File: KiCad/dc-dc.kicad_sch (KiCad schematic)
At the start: 60 parts, among them Q1 NMOS, Q2 NMOS, Q3 NMOS, Q4 NMOS, U3 LT8390xFE

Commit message: new layout
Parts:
- removed NT1, NT2, NT3, NT4: NetTie_2, symbol Device:NetTie_2
- removed R5: 5m, Resistor_SMD:R_1206_3216Metric, symbol Device:R
- removed R6: 20m, Resistor_SMD:R_1206_3216Metric, symbol Device:R
- added HS1: 960-21-18-D-AB-0, Library:960-21-xx-D, symbol Mechanical:Heatsink
- added R5: 5m, Resistor_SMD:R_Shunt_Ohmite_LVK12, symbol Device:R_Shunt
- added R6: 12m, Resistor_SMD:R_Shunt_Ohmite_LVK12, symbol Device:R_Shunt
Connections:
- net ISN: now also R6.3
- net ISP: now also R6.2
- net LSN: now also R5.2
- net LSP: now also R5.3
- net SW1: now also R5.4
- net VOUT: now also R6.4
- net VOUTa: now reaches C15.1, C16.1, C17.1, C18.1, C19.1, Q3.1 (D)
- net VOUTa: now also R6.1
- net SW1a: now reaches L1.1
- net SW1a: now also R5.1

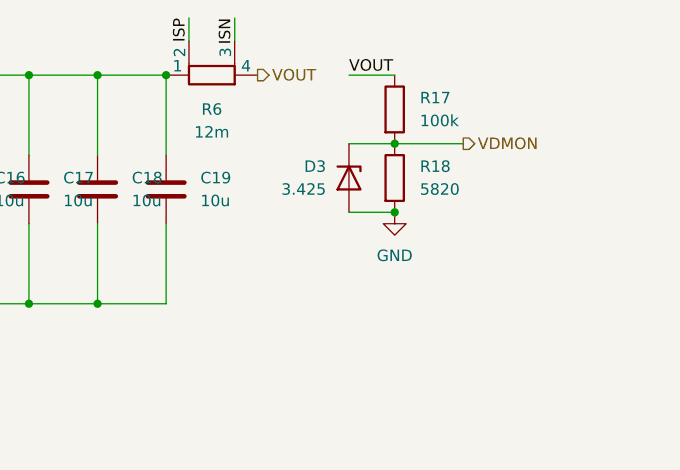
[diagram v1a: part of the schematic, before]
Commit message: multi sheet redesign
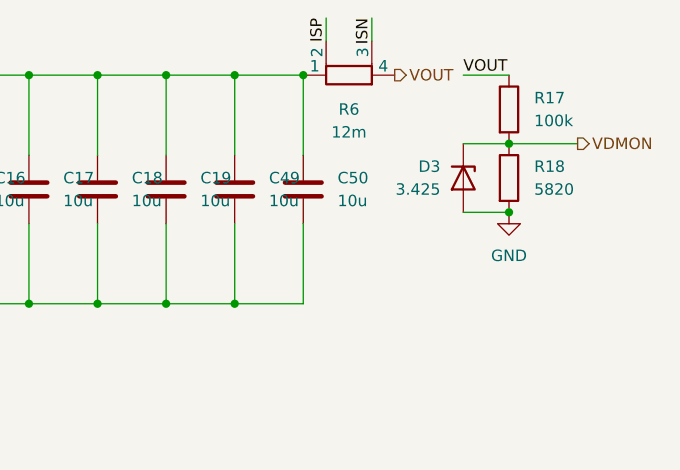
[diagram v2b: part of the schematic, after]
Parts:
- added C49, C50: 10u, Capacitor_SMD:C_1206_3216Metric, symbol Device:C
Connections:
- net GND: now also C49.2, C50.2
- net VOUTa: now also C49.1, C50.1
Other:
- moved on the sheet: D3, R17, R18, R6

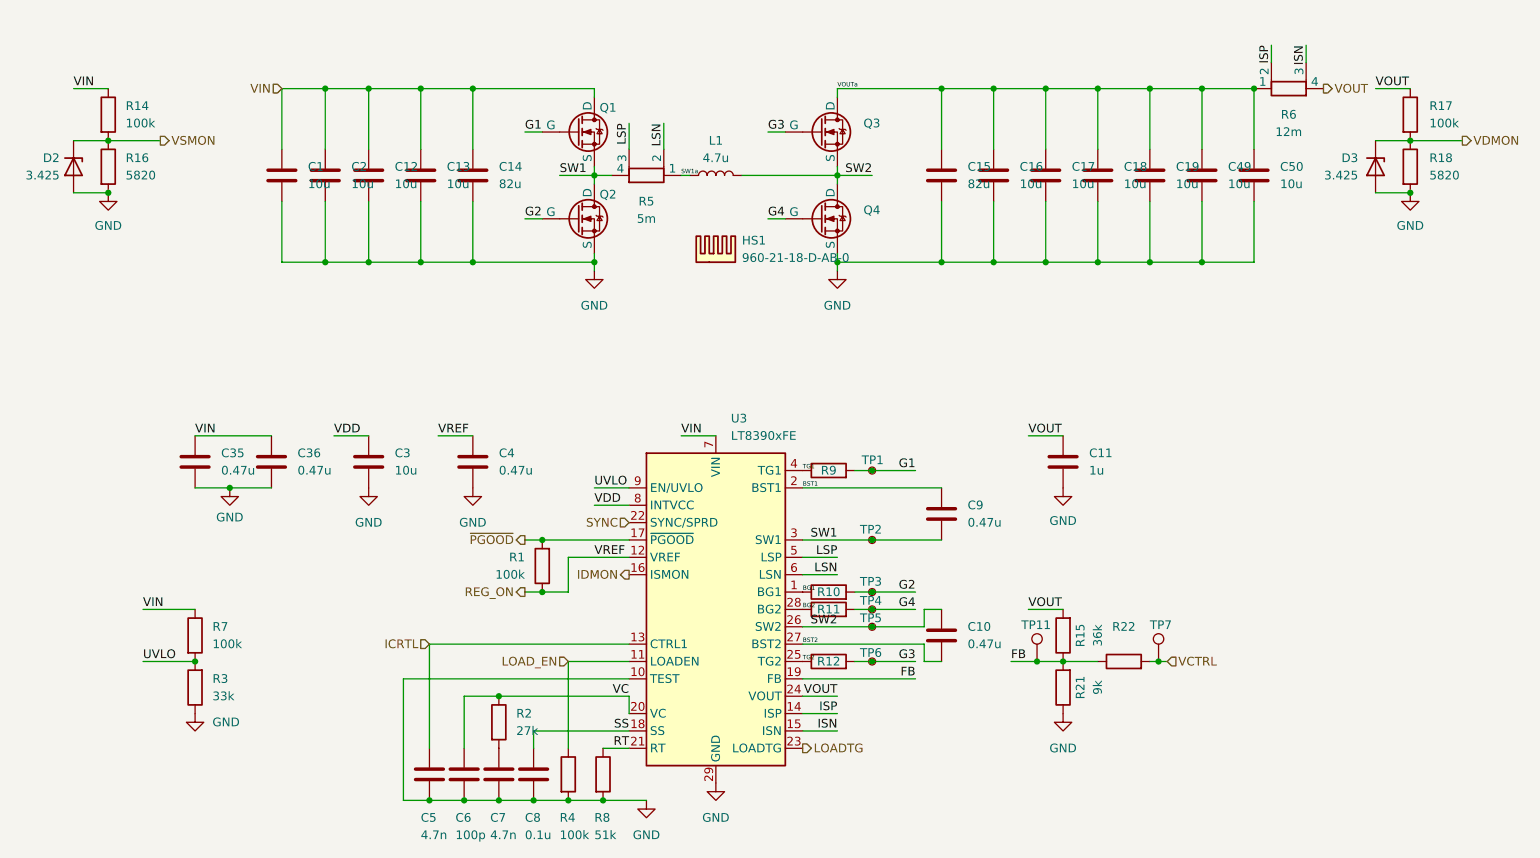
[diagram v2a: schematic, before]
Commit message: standalone regulator core
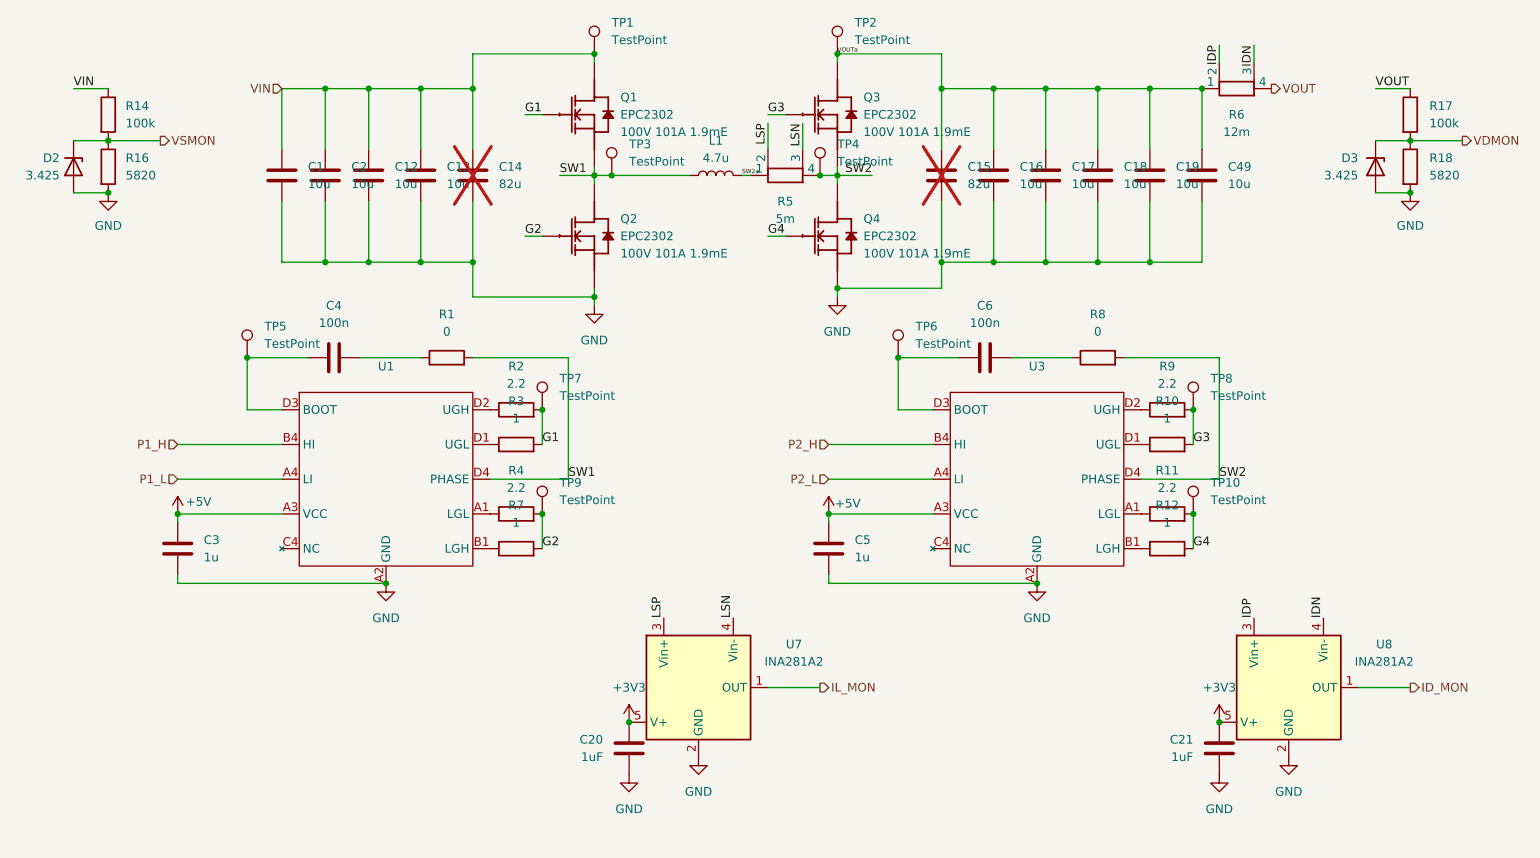
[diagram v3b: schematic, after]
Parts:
- removed C10, C35, C36, C9: 0.47u, Capacitor_SMD:C_0805_2012Metric, symbol Device:C
- removed C11: 1u, Capacitor_SMD:C_0603_1608Metric, symbol Device:C
- removed C50: 10u, Capacitor_SMD:C_1206_3216Metric, symbol Device:C
- removed C7: 4.7n, Capacitor_SMD:C_0603_1608Metric, symbol Device:C
- removed C8: 0.1u, Capacitor_SMD:C_0603_1608Metric, symbol Device:C
- removed HS1: 960-21-18-D-AB-0, Library:960-21-xx-D, symbol Mechanical:Heatsink
- removed Q1, Q2, Q3, Q4: NMOS, Library:ECP2302, symbol Simulation_SPICE:NMOS
- removed R15: 36k, Resistor_SMD:R_0603_1608Metric, symbol Device:R
- removed R21: 9k, Resistor_SMD:R_0603_1608Metric, symbol Device:R
- removed R22: ~, Resistor_SMD:R_0603_1608Metric, symbol Device:R
- removed TP1, TP2, TP3, TP4, TP5, TP6: TestPoint_Small, TestPoint:TestPoint_Pad_D1.0mm, symbol Connector:TestPoint_Small
- removed TP11: TestPoint_Small, TestPoint:TestPoint_Pad_D1.0mm, symbol Connector:TestPoint
- removed U3: LT8390xFE, Package_SO:TSSOP-28-1EP_4.4x9.7mm_P0.65mm, symbol Driver_LED:LT8391xFE
- added C20, C21: 1uF, Capacitor_SMD:C_0603_1608Metric, symbol Device:C
- added Q1, Q2, Q3, Q4: EPC2302, KiFootprints:D0606F_100V, symbol EPC_FETs:EPC2302
- added TP1, TP2, TP3, TP4: TestPoint, TestPoint:TestPoint_Keystone_5000-5004_Miniature, symbol Connector:TestPoint
- added TP10, TP5, TP6, TP8, TP9: TestPoint, TestPoint:TestPoint_Pad_D1.0mm, symbol Connector:TestPoint
- added U1, U3: ~, KiFootprints:WLCSP1.6x1.6-12B, symbol EPC_FETs:uP1966E
- added U7, U8: INA281A2, Package_TO_SOT_SMD:SOT-23-5, symbol Amplifier_Current:INA281A2
- C14, C15: now not fitted
- C3: value 10u -> 1u; footprint Capacitor_SMD:C_1206_3216Metric -> Capacitor_SMD:C_0402_1005Metric
- C4: value 0.47u -> 100n; footprint Capacitor_SMD:C_0603_1608Metric -> Capacitor_SMD:C_0402_1005Metric
- C5: value 4.7n -> 1u; footprint Capacitor_SMD:C_0603_1608Metric -> Capacitor_SMD:C_0402_1005Metric
- C6: value 100p -> 100n; footprint Capacitor_SMD:C_0603_1608Metric -> Capacitor_SMD:C_0402_1005Metric
- R1: value 100k -> 0; footprint Resistor_SMD:R_0603_1608Metric -> Resistor_SMD:R_0402_1005Metric
- R10, R12: footprint Resistor_SMD:R_0603_1608Metric -> Resistor_SMD:R_0402_1005Metric
- R11, R9: value 1 -> 2.2; footprint Resistor_SMD:R_0603_1608Metric -> Resistor_SMD:R_0402_1005Metric
- R2: value 27k -> 2.2; footprint Resistor_SMD:R_0603_1608Metric -> Resistor_SMD:R_0402_1005Metric
- R3: value 33k -> 1; footprint Resistor_SMD:R_0603_1608Metric -> Resistor_SMD:R_0402_1005Metric
- R4: value 100k -> 2.2; footprint Resistor_SMD:R_0603_1608Metric -> Resistor_SMD:R_0402_1005Metric
- R7: value 100k -> 1; footprint Resistor_SMD:R_0603_1608Metric -> Resistor_SMD:R_0402_1005Metric
- R8: value 51k -> 0; footprint Resistor_SMD:R_0603_1608Metric -> Resistor_SMD:R_0402_1005Metric
- TP7: value TestPoint_Small -> TestPoint; now left out of the parts list
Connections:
- net VCTRL is gone; now on net G1: TP7.1
- net VDD is gone; now on net +5V: C3.1
- net ~{PGOOD} is gone; now on net SW1: R1.2
- net G1: now also R2.2, R3.2, Q1.1 (G); no longer R9.2
- net G2: now also R4.2, R7.2, Q2.1 (G), TP9.1; no longer R10.2
- net G3: now also R10.2, R9.2, Q3.1 (G), TP8.1; no longer R12.2
- net G4: now also R12.2, Q4.1 (G), TP10.1
- net GND: now also C20.2, C21.2, Q2.2 (S), Q2.4 (S), Q2.6 (S), Q4.2 (S), Q4.4 (S), Q4.6 (S), U1.A2 (GND), U3.A2 (GND), U7.2 (GND), U8.2 (GND); no longer C4.2, C6.2, R3.1, R4.2, R8.2
- net LSN: now also R5.3, U7.4 (Vin-); no longer R5.2
- net LSP: now also R5.2, U7.3 (Vin+); no longer R5.3
- net SW1: now also L1.1, Q1.2 (S), Q1.4 (S), Q1.6 (S), Q2.3 (D), Q2.5 (D), Q2.7 (D), TP3.1, U1.C1 (PHASE), U1.D4 (PHASE); no longer R5.4
- net SW2: now also R5.4, R8.2, Q3.2 (S), Q3.4 (S), Q3.6 (S), Q4.3 (D), Q4.5 (D), Q4.7 (D), TP4.1, U3.C1 (PHASE), U3.D4 (PHASE); no longer L1.2
- net VIN: now also Q1.3 (D), Q1.5 (D), Q1.7 (D), TP1.1; no longer R7.1
- net VOUTa: now also Q3.3 (D), Q3.5 (D), Q3.7 (D), TP2.1
- net BG1: no longer names the net of R10.1
- net BG1: now also U3.D1 (UGL)
- net BG2: no longer names the net of R11.1
- net BG2: now also U3.A1 (LGL)
- net ICRTL renamed +5V
- net +5V: now also U1.A3 (VCC), U3.A3 (VCC)
- net ISN renamed IDN
- net IDN: now also U8.4 (Vin-)
- net ISP renamed IDP
- net IDP: now also U8.3 (Vin+)
- net LOAD_EN: no longer names the net of R4.1
- net LOAD_EN: now also U1.A1 (LGL)
- net REG_ON: no longer names the net of C4.1
- net REG_ON: now also TP5.1, U1.D3 (BOOT); no longer R1.1
- net RT: no longer names the net of R8.1
- net RT: now also C6.2
- net SW1a renamed SW2a
- net SW2a: now also L1.2; no longer L1.1
- net TG1: no longer names the net of R9.1
- net TG1: now also U3.D2 (UGH)
- net TG2: no longer names the net of R12.1
- net TG2: now also U3.B1 (LGH)
- removed net UVLO: R3.2, R7.2
- net VC: no longer names the net of R2.1
- net VC: now also U1.D2 (UGH); no longer C6.1
- new net: R7.1, U1.B1 (LGH)
- new net: R3.1, U1.D1 (UGL)
- new net: C4.2, R1.1
- new net: C6.1, TP6.1, U3.D3 (BOOT)
- new net +3V3: C20.1, C21.1, U7.5 (V+), U8.5 (V+)
- new net ID_MON: U8.1 (OUT)
- new net IL_MON: U7.1 (OUT)
- new net P1_H: U1.B4 (HI)
- new net P1_L: U1.A4 (LI)
- new net P2_H: U3.B4 (HI)
- new net P2_L: U3.A4 (LI)
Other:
- moved on the sheet: R5, R6
